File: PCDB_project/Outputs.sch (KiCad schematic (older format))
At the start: 14 parts, among them J3 22-05-7025, J4 22-05-7025, J5 22-05-7025, U6 MC74LCX0

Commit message: BOM añadido y comprobado las footprints, en principio estan bien. falta ocnfirmar con el profesor y medir el boton que parece que no estoy seguro si están bien hechos los pines
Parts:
- J3, J4, J5: footprint (none) -> PCDB_project:IO2
- U6: footprint (none) -> Package_SO:SOIC-14_3.9x8.7mm_P1.27mm
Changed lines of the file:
@@
 F 0 "U6" H 3750 3017 50  0000 C CNN
 F 1 "MC74LCX0" H 3750 2926 50  0000 C CNN
-F 2 "" H 3750 2700 50  0001 C CNN
+F 2 "Package_SO:SOIC-14_3.9x8.7mm_P1.27mm" H 3750 2700 50  0001 C CNN
 F 3 "http://www.ti.com/lit/gpn/sn74LS06" H 3750 2700 50  0001 C CNN
 F 4 "MC74LCX07" H 3750 2700 50  0001 C CNN "Name"
@@
 F 0 "U6" H 3750 3567 50  0000 C CNN
 F 1 "MC74LCX0" H 3750 3476 50  0000 C CNN
-F 2 "" H 3750 3250 50  0001 C CNN
+F 2 "Package_SO:SOIC-14_3.9x8.7mm_P1.27mm" H 3750 3250 50  0001 C CNN
 F 3 "http://www.ti.com/lit/gpn/sn74LS06" H 3750 3250 50  0001 C CNN
 F 4 "MC74LCX07" H 3750 3250 50  0001 C CNN "Name"
@@
 F 0 "U6" H 3750 4117 50  0000 C CNN
 F 1 "MC74LCX0" H 3750 4026 50  0000 C CNN
-F 2 "" H 3750 3800 50  0001 C CNN
+F 2 "Package_SO:SOIC-14_3.9x8.7mm_P1.27mm" H 3750 3800 50  0001 C CNN
 F 3 "http://www.ti.com/lit/gpn/sn74LS06" H 3750 3800 50  0001 C CNN
 F 4 "MC74LCX07" H 3750 3800 50  0001 C CNN "Name"
@@
 F 0 "U6" H 3750 4667 50  0000 C CNN
 F 1 "MC74LCX0" H 3750 4576 50  0000 C CNN
-F 2 "" H 3750 4350 50  0001 C CNN
+F 2 "Package_SO:SOIC-14_3.9x8.7mm_P1.27mm" H 3750 4350 50  0001 C CNN
 F 3 "http://www.ti.com/lit/gpn/sn74LS06" H 3750 4350 50  0001 C CNN
 F 4 "MC74LCX07" H 3750 4350 50  0001 C CNN "Name"
@@
 F 0 "U6" H 3750 5217 50  0000 C CNN
 F 1 "MC74LCX0" H 3750 5126 50  0000 C CNN
-F 2 "" H 3750 4900 50  0001 C CNN
+F 2 "Package_SO:SOIC-14_3.9x8.7mm_P1.27mm" H 3750 4900 50  0001 C CNN
 F 3 "http://www.ti.com/lit/gpn/sn74LS06" H 3750 4900 50  0001 C CNN
 F 4 "MC74LCX07" H 3750 4900 50  0001 C CNN "Name"
@@
 F 0 "U6" H 3750 5767 50  0000 C CNN
 F 1 "MC74LCX0" H 3750 5676 50  0000 C CNN
-F 2 "" H 3750 5450 50  0001 C CNN
+F 2 "Package_SO:SOIC-14_3.9x8.7mm_P1.27mm" H 3750 5450 50  0001 C CNN
 F 3 "http://www.ti.com/lit/gpn/sn74LS06" H 3750 5450 50  0001 C CNN
 F 4 "MC74LCX07" H 3750 5450 50  0001 C CNN "Name"
@@
 F 0 "U6" H 1930 1946 50  0000 L CNN
 F 1 "MC74LCX0" H 1930 1855 50  0000 L CNN
-F 2 "" H 1700 1900 50  0001 C CNN
+F 2 "Package_SO:SOIC-14_3.9x8.7mm_P1.27mm" H 1700 1900 50  0001 C CNN
 F 3 "http://www.ti.com/lit/gpn/sn74LS06" H 1700 1900 50  0001 C CNN
 	7    1700 1900
@@
 F 0 "J3" H 8130 3242 50  0000 L CNN
 F 1 "22-05-7025" H 8130 3151 50  0000 L CNN
-F 2 "" H 8050 3250 50  0001 C CNN
+F 2 "PCDB_project:IO2" H 8050 3250 50  0001 C CNN
 F 3 "~" H 8050 3250 50  0001 C CNN
 F 4 "22-05-7025" H 8050 3250 50  0001 C CNN "Name"
@@
 F 0 "J4" H 8130 4342 50  0000 L CNN
 F 1 "22-05-7025" H 8130 4251 50  0000 L CNN
-F 2 "" H 8050 4350 50  0001 C CNN
+F 2 "PCDB_project:IO2" H 8050 4350 50  0001 C CNN
 F 3 "~" H 8050 4350 50  0001 C CNN
 F 4 "22-05-7025" H 8050 4350 50  0001 C CNN "Name"
@@
 F 0 "J5" H 8130 5442 50  0000 L CNN
 F 1 "22-05-7025" H 8130 5351 50  0000 L CNN
-F 2 "" H 8050 5450 50  0001 C CNN
+F 2 "PCDB_project:IO2" H 8050 5450 50  0001 C CNN
 F 3 "~" H 8050 5450 50  0001 C CNN
 F 4 "22-05-7025" H 8050 5450 50  0001 C CNN "Name"

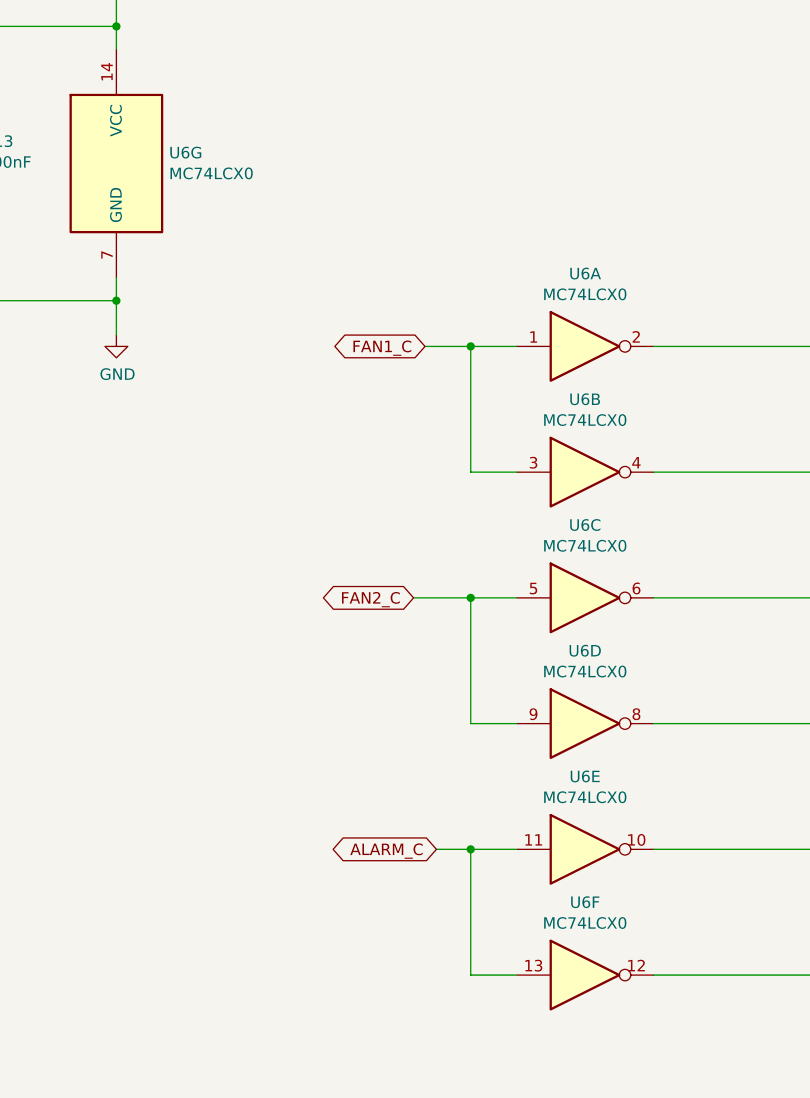
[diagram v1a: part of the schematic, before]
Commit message: Primera version de placement, bom coregido y footprints corregidas y verificadas
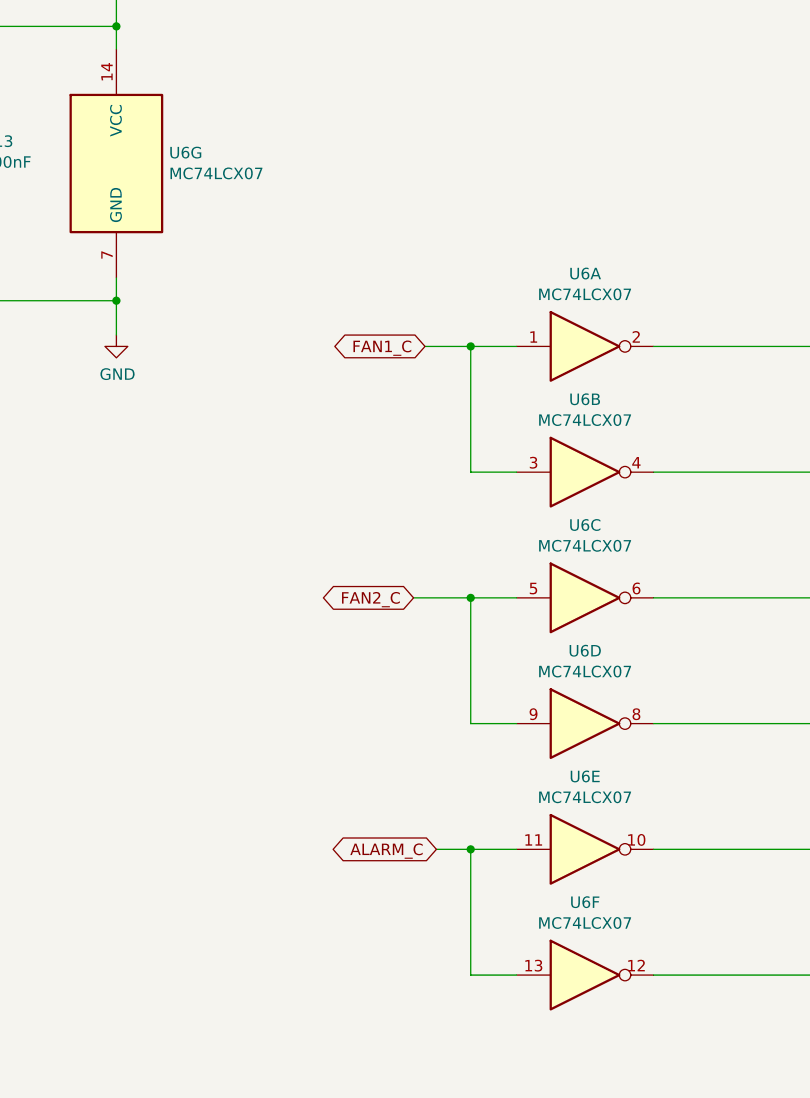
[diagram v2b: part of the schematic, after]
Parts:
- U6: value MC74LCX0 -> MC74LCX07
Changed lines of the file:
@@
 P 3750 2700
 F 0 "U6" H 3750 3017 50  0000 C CNN
-F 1 "MC74LCX0" H 3750 2926 50  0000 C CNN
+F 1 "MC74LCX07" H 3750 2926 50  0000 C CNN
 F 2 "Package_SO:SOIC-14_3.9x8.7mm_P1.27mm" H 3750 2700 50  0001 C CNN
 F 3 "http://www.ti.com/lit/gpn/sn74LS06" H 3750 2700 50  0001 C CNN
@@
 P 3750 3250
 F 0 "U6" H 3750 3567 50  0000 C CNN
-F 1 "MC74LCX0" H 3750 3476 50  0000 C CNN
+F 1 "MC74LCX07" H 3750 3476 50  0000 C CNN
 F 2 "Package_SO:SOIC-14_3.9x8.7mm_P1.27mm" H 3750 3250 50  0001 C CNN
 F 3 "http://www.ti.com/lit/gpn/sn74LS06" H 3750 3250 50  0001 C CNN
@@
 P 3750 3800
 F 0 "U6" H 3750 4117 50  0000 C CNN
-F 1 "MC74LCX0" H 3750 4026 50  0000 C CNN
+F 1 "MC74LCX07" H 3750 4026 50  0000 C CNN
 F 2 "Package_SO:SOIC-14_3.9x8.7mm_P1.27mm" H 3750 3800 50  0001 C CNN
 F 3 "http://www.ti.com/lit/gpn/sn74LS06" H 3750 3800 50  0001 C CNN
@@
 P 3750 4350
 F 0 "U6" H 3750 4667 50  0000 C CNN
-F 1 "MC74LCX0" H 3750 4576 50  0000 C CNN
+F 1 "MC74LCX07" H 3750 4576 50  0000 C CNN
 F 2 "Package_SO:SOIC-14_3.9x8.7mm_P1.27mm" H 3750 4350 50  0001 C CNN
 F 3 "http://www.ti.com/lit/gpn/sn74LS06" H 3750 4350 50  0001 C CNN
@@
 P 3750 4900
 F 0 "U6" H 3750 5217 50  0000 C CNN
-F 1 "MC74LCX0" H 3750 5126 50  0000 C CNN
+F 1 "MC74LCX07" H 3750 5126 50  0000 C CNN
 F 2 "Package_SO:SOIC-14_3.9x8.7mm_P1.27mm" H 3750 4900 50  0001 C CNN
 F 3 "http://www.ti.com/lit/gpn/sn74LS06" H 3750 4900 50  0001 C CNN
@@
 P 3750 5450
 F 0 "U6" H 3750 5767 50  0000 C CNN
-F 1 "MC74LCX0" H 3750 5676 50  0000 C CNN
+F 1 "MC74LCX07" H 3750 5676 50  0000 C CNN
 F 2 "Package_SO:SOIC-14_3.9x8.7mm_P1.27mm" H 3750 5450 50  0001 C CNN
 F 3 "http://www.ti.com/lit/gpn/sn74LS06" H 3750 5450 50  0001 C CNN
@@
 P 1700 1900
 F 0 "U6" H 1930 1946 50  0000 L CNN
-F 1 "MC74LCX0" H 1930 1855 50  0000 L CNN
+F 1 "MC74LCX07" H 1930 1855 50  0000 L CNN
 F 2 "Package_SO:SOIC-14_3.9x8.7mm_P1.27mm" H 1700 1900 50  0001 C CNN
 F 3 "http://www.ti.com/lit/gpn/sn74LS06" H 1700 1900 50  0001 C CNN
